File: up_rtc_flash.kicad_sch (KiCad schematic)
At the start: 0 parts

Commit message: add comments/todos for each schematics page
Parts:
- added Card?: PCIE-52P40H, PCIE-SMD_PCIE-52P40H, symbol eduboardv2:PCIE-52P40H
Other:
- note added: "UP-Connector, RTC and Flash - UP-Connector M.2: PCIE-52P40H - RTC: DS1307 (I2C) - CR2032 Battery: CR2032-BS-6-1 - Flash: W25Q128JVSIQ (Dual/Quad-SPI)"
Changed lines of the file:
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@@
     (company "Juventus Technikerschule")
   )
+  (text "UP-Connector, RTC and Flash\n- UP-Connector M.2: PCIE-52P40H\n- RTC: DS1307 (I2C)\n- CR2032 Battery: CR2032-BS-6-1\n- Flash: W25Q128JVSIQ (Dual/Quad-SPI)"
+    (at 13.97 24.13 0)
+    (effects (font (size 1.27 1.27)) (justify left bottom))
+  )
+  (symbol (lib_id "eduboardv2:PCIE-52P40H") (at 63.5 77.47 270) (unit 1)
+    (in_bom yes) (on_board yes) (fields_autoplaced)
+    (property "Reference" "Card?" (id 0) (at 66.2687 38.3372 90)
+      (effects (font (size 1.27 1.27)) (justify left))
+    )
+    (property "Value" "PCIE-52P40H" (id 1) (at 66.2687 40.8741 90)
+      (effects (font (size 1.27 1.27)) (justify left))
+    )
+    (property "Footprint" "PCIE-SMD_PCIE-52P40H" (id 2) (at 48.26 77.47 0)
+      (effects (font (size 1.27 1.27)) hide)
+    )
+    (property "Datasheet" "https://lcsc.com/product-detail/Connector-Card-Sockets_XUNPU-PCIE-52P40H_C266898.html" (id 3) (at 45.72 77.47 0)
+      (effects (font (size 1.27 1.27)) hide)
+    )
+    (property "Manufacturer" "XUNPU" (id 4) (at 43.18 77.47 0)
+      (effects (font (size 1.27 1.27)) hide)
+    )
+    (property "LCSC Part" "C266898" (id 5) (at 40.64 77.47 0)
+      (effects (font (size 1.27 1.27)) hide)
+    )
+    (property "JLC Part" "Extended Part" (id 6) (at 38.1 77.47 0)
+      (effects (font (size 1.27 1.27)) hide)
+    )
+    (pin "1")
+    (pin "10")
+    (pin "11")
+    (pin "12")
+    (pin "13")
+    (pin "14")
+    (pin "15")
+    (pin "16")
+    (pin "17")
+    (pin "18")
+    (pin "19")
+    (pin "2")
+    (pin "20")
+    (pin "21")
+    (pin "22")
+    (pin "23")
+    (pin "24")
+    (pin "25")
+    (pin "26")
+    (pin "27")
+    (pin "28")
+    (pin "29")
+    (pin "3")
+    (pin "30")
+    (pin "31")
+    (pin "32")
+    (pin "33")
+    (pin "34")
+    (pin "35")
+    (pin "36")
+    (pin "37")
+    (pin "38")
+    (pin "39")
+    (pin "4")
+    (pin "40")
+    (pin "41")
+    (pin "42")
+    (pin "43")
+    (pin "44")
+    (pin "45")
+    (pin "46")
+    (pin "47")
+    (pin "48")
+    (pin "49")
+    (pin "5")
+    (pin "50")
+    (pin "51")
+    (pin "52")
+    (pin "53")
+    (pin "54")
+    (pin "6")
+    (pin "7")
+    (pin "8")
+    (pin "9")
+  )
 )

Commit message: updated library, partly created power.kicad_sch
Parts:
- gave numbers to parts that had none: 1
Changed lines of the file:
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@@
   (symbol (lib_id "eduboardv2:PCIE-52P40H") (at 63.5 77.47 270) (unit 1)
     (in_bom yes) (on_board yes) (fields_autoplaced)
-    (property "Reference" "Card?" (id 0) (at 66.2687 38.3372 90)
+    (property "Reference" "X201" (id 0) (at 66.2687 36.83 90)
       (effects (font (size 1.27 1.27)) (justify left))
     )
-    (property "Value" "PCIE-52P40H" (id 1) (at 66.2687 40.8741 90)
+    (property "Value" "PCIE-52P40H" (id 1) (at 66.2687 39.37 90)
       (effects (font (size 1.27 1.27)) (justify left))
     )

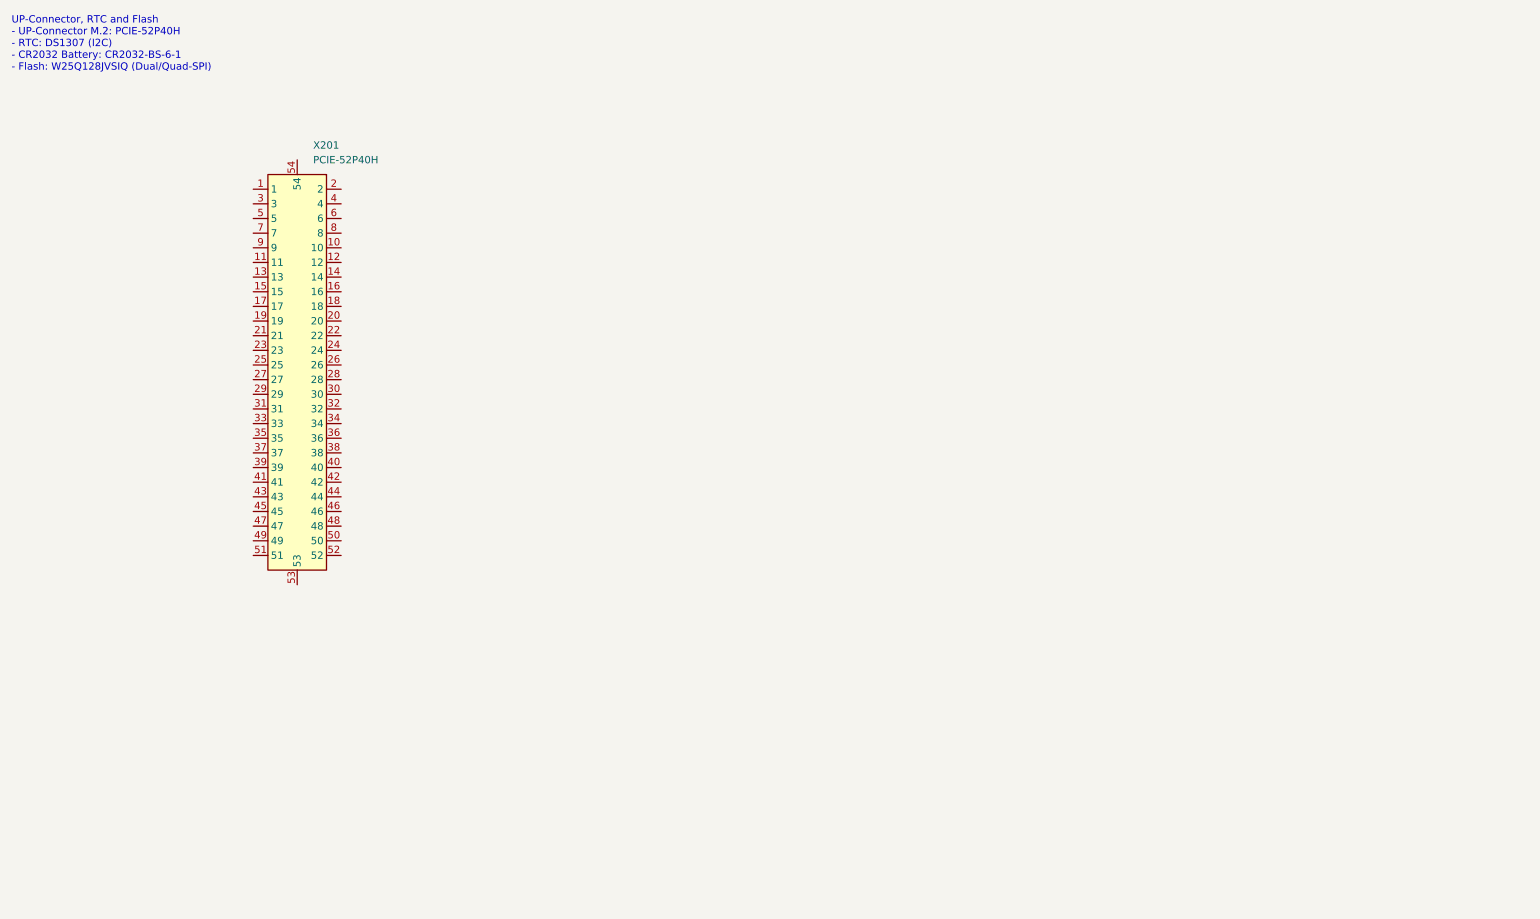
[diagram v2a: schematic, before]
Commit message: added up_rtc_flash.kicad_sch and finished others
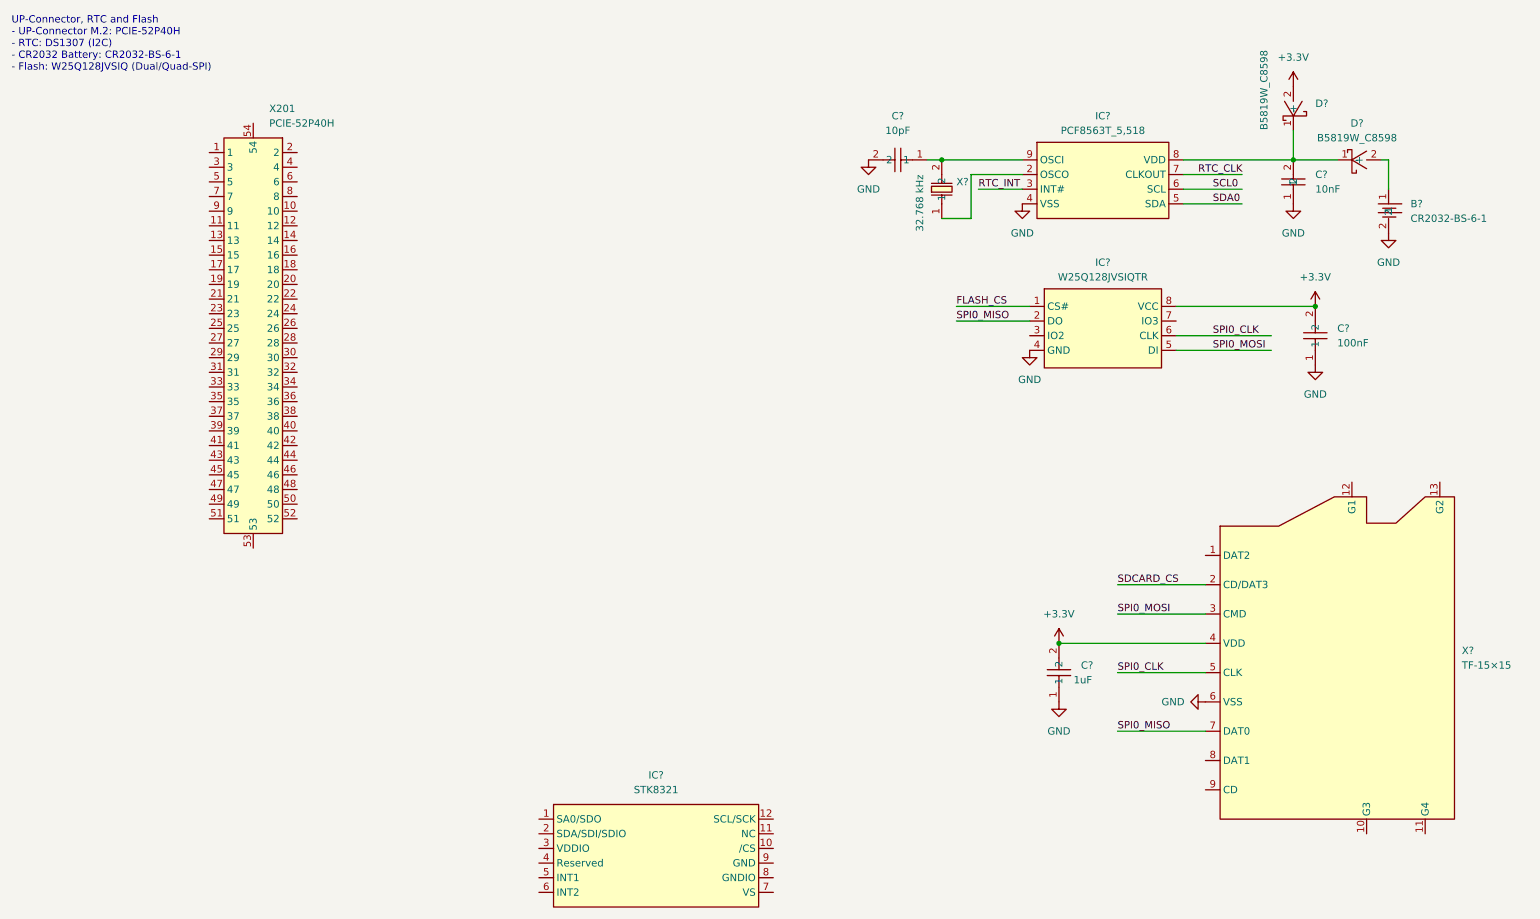
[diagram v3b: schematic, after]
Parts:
- added B?: CR2032-BS-6-1, BAT-TH_CR2032-BS-6-1, symbol eduboardv2:CR2032-BS-6-1
- added C?: 10pF, C0402, symbol eduboardv2:CL05C100JB5NNNC
- added C?: 10nF, C0402, symbol eduboardv2:CL05B103KB5NNNC
- added C?: 1uF, C0402, symbol eduboardv2:CL05A105KA5NQNC
- added C?: 100nF, C0402, symbol eduboardv2:CL05B104KB54PNC
- added D? (x2): B5819W_C8598, SOD-123_L2.7-W1.6-LS3.7-RD-1, symbol eduboardv2:B5819W_C8598
- added IC?: STK8321, LGA-12_L2.0-W2.0-P0.50-TR, symbol eduboardv2:STK8321
- added IC?: W25Q128JVSIQTR, SOIC-8_L5.3-W5.3-P1.27-LS8.0-BL, symbol eduboardv2:W25Q128JVSIQTR
- added IC?: PCF8563T_5,518, SOIC-8_L5.0-W4.0-P1.27-LS6.0-BL, symbol eduboardv2:PCF8563T_5,518
- added X?: TF-15×15, TF-SMD_TF-15-15, symbol eduboardv2:TF-15×15
- added X?: 32.768 kHz, FC-135R_L3.2-W1.5, symbol eduboardv2:Q13FC1350000400
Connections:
- new net: C?.2, D?.1 (-), D?.1 (-), IC?.8 (VDD)
- new net: B?.1, D?.2 (+)
- new net: C?.1, IC?.9 (OSCI), X?.2
- new net: IC?.2 (OSCO), X?.1
- new net +3.3V: C?.2, C?.2, D?.2 (+), IC?.8 (VCC), X?.4 (VDD)
- new net FLASH_CS: IC?.1 (CS#)
- new net GND: B?.2, C?.1, C?.1, C?.1, C?.2, IC?.4 (GND), IC?.4 (VSS), X?.6 (VSS)
- new net RTC_CLK: IC?.7 (CLKOUT)
- new net RTC_INT: IC?.3 (INT#)
- new net SCL0: IC?.6 (SCL)
- new net SDA0: IC?.5 (SDA)
- new net SDCARD_CS: X?.2 (CD/DAT3)
- new net SPI0_CLK: IC?.6 (CLK), X?.5 (CLK)
- new net SPI0_MISO: IC?.2 (DO), X?.7 (DAT0)
- new net SPI0_MOSI: IC?.5 (DI), X?.3 (CMD)
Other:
- moved on the sheet: X201

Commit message: added more components
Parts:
- gave numbers to parts that had none: 12
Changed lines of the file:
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@@
   (symbol (lib_id "eduboardv2:STK8321") (at 125.73 160.02 0) (unit 1)
     (in_bom yes) (on_board yes) (fields_autoplaced)
-    (property "Reference" "IC?" (id 0) (at 125.73 146.05 0))
+    (property "Reference" "IC201" (id 0) (at 125.73 146.05 0))
     (property "Value" "STK8321" (id 1) (at 125.73 148.59 0))
     (property "Footprint" "LGA-12_L2.0-W2.0-P0.50-TR" (id 2) (at 125.73 173.99 0)
@@
   (symbol (lib_id "eduboardv2:B5819W_C8598") (at 247.65 39.37 0) (unit 1)
     (in_bom yes) (on_board yes) (fields_autoplaced)
-    (property "Reference" "D?" (id 0) (at 247.269 33.02 0))
+    (property "Reference" "D202" (id 0) (at 247.269 33.02 0))
     (property "Value" "B5819W_C8598" (id 1) (at 247.269 35.56 0))
     (property "Footprint" "SOD-123_L2.7-W1.6-LS3.7-RD-1" (id 2) (at 247.65 46.99 0)
@@
   (symbol (lib_id "power:GND") (at 220.98 133.35 270) (unit 1)
     (in_bom yes) (on_board yes)
-    (property "Reference" "#PWR?" (id 0) (at 214.63 133.35 0)
+    (property "Reference" "#PWR0206" (id 0) (at 214.63 133.35 0)
       (effects (font (size 1.27 1.27)) hide)
     )
@@
   (symbol (lib_id "eduboardv2:W25Q128JVSIQTR") (at 203.2 68.58 0) (unit 1)
     (in_bom yes) (on_board yes) (fields_autoplaced)
-    (property "Reference" "IC?" (id 0) (at 203.2 57.15 0))
+    (property "Reference" "IC203" (id 0) (at 203.2 57.15 0))
     (property "Value" "W25Q128JVSIQTR" (id 1) (at 203.2 59.69 0))
     (property "Footprint" "SOIC-8_L5.3-W5.3-P1.27-LS8.0-BL" (id 2) (at 203.2 80.01 0)
@@
   (symbol (lib_id "power:GND") (at 190.5 72.39 0) (unit 1)
     (in_bom yes) (on_board yes) (fields_autoplaced)
-    (property "Reference" "#PWR?" (id 0) (at 190.5 78.74 0)
+    (property "Reference" "#PWR0203" (id 0) (at 190.5 78.74 0)
       (effects (font (size 1.27 1.27)) hide)
     )
@@
   (symbol (lib_id "eduboardv2:CL05C100JB5NNNC") (at 167.64 39.37 180) (unit 1)
     (in_bom yes) (on_board yes) (fields_autoplaced)
-    (property "Reference" "C?" (id 0) (at 167.64 31.75 0))
+    (property "Reference" "C201" (id 0) (at 167.64 31.75 0))
     (property "Value" "10pF" (id 1) (at 167.64 34.29 0))
     (property "Footprint" "C0402" (id 2) (at 167.64 31.75 0)
@@
   (symbol (lib_id "eduboardv2:CR2032-BS-6-1") (at 252.73 48.26 270) (unit 1)
     (in_bom yes) (on_board yes) (fields_autoplaced)
-    (property "Reference" "B?" (id 0) (at 256.54 46.9899 90)
+    (property "Reference" "B201" (id 0) (at 256.54 46.9899 90)
       (effects (font (size 1.27 1.27)) (justify left))
     )
@@
   (symbol (lib_id "eduboardv2:CL05B103KB5NNNC") (at 236.22 43.18 90) (unit 1)
     (in_bom yes) (on_board yes) (fields_autoplaced)
-    (property "Reference" "C?" (id 0) (at 240.03 41.9099 90)
+    (property "Reference" "C203" (id 0) (at 240.03 41.9099 90)
       (effects (font (size 1.27 1.27)) (justify right))
     )
@@
   (symbol (lib_id "power:GND") (at 189.23 46.99 0) (unit 1)
     (in_bom yes) (on_board yes) (fields_autoplaced)
-    (property "Reference" "#PWR?" (id 0) (at 189.23 53.34 0)
+    (property "Reference" "#PWR0202" (id 0) (at 189.23 53.34 0)
       (effects (font (size 1.27 1.27)) hide)
     )
@@
   (symbol (lib_id "eduboardv2:CL05A105KA5NQNC") (at 195.58 128.27 90) (unit 1)
     (in_bom yes) (on_board yes)
-    (property "Reference" "C?" (id 0) (at 199.39 126.9999 90)
+    (property "Reference" "C202" (id 0) (at 199.39 126.9999 90)
       (effects (font (size 1.27 1.27)) (justify right))
     )
@@
   (symbol (lib_id "eduboardv2:B5819W_C8598") (at 236.22 30.48 90) (unit 1)
     (in_bom yes) (on_board yes)
-    (property "Reference" "D?" (id 0) (at 240.03 29.5909 90)
+    (property "Reference" "D201" (id 0) (at 240.03 29.5909 90)
       (effects (font (size 1.27 1.27)) (justify right))
     )
@@
   (symbol (lib_id "power:+3.3V") (at 240.03 64.77 0) (unit 1)
     (in_bom yes) (on_board yes) (fields_autoplaced)
-    (property "Reference" "#PWR?" (id 0) (at 240.03 68.58 0)
+    (property "Reference" "#PWR0209" (id 0) (at 240.03 68.58 0)
       (effects (font (size 1.27 1.27)) hide)
     )
@@
   (symbol (lib_id "power:+3.3V") (at 195.58 123.19 0) (unit 1)
     (in_bom yes) (on_board yes) (fields_autoplaced)
-    (property "Reference" "#PWR?" (id 0) (at 195.58 127 0)
+    (property "Reference" "#PWR0204" (id 0) (at 195.58 127 0)
       (effects (font (size 1.27 1.27)) hide)
     )
@@
   (symbol (lib_id "power:GND") (at 162.56 39.37 0) (unit 1)
     (in_bom yes) (on_board yes) (fields_autoplaced)
-    (property "Reference" "#PWR?" (id 0) (at 162.56 45.72 0)
+    (property "Reference" "#PWR0201" (id 0) (at 162.56 45.72 0)
       (effects (font (size 1.27 1.27)) hide)
     )
@@
   (symbol (lib_id "eduboardv2:TF-15×15") (at 240.03 125.73 0) (unit 1)
     (in_bom yes) (on_board yes) (fields_autoplaced)
-    (property "Reference" "X?" (id 0) (at 265.43 124.4599 0)
+    (property "Reference" "X203" (id 0) (at 265.43 124.4599 0)
       (effects (font (size 1.27 1.27)) (justify left))
     )
@@
   (symbol (lib_id "power:+3.3V") (at 236.22 26.67 0) (unit 1)
     (in_bom yes) (on_board yes) (fields_autoplaced)
-    (property "Reference" "#PWR?" (id 0) (at 236.22 30.48 0)
+    (property "Reference" "#PWR0207" (id 0) (at 236.22 30.48 0)
       (effects (font (size 1.27 1.27)) hide)
     )
@@
   (symbol (lib_id "power:GND") (at 240.03 74.93 0) (unit 1)
     (in_bom yes) (on_board yes) (fields_autoplaced)
-    (property "Reference" "#PWR?" (id 0) (at 240.03 81.28 0)
+    (property "Reference" "#PWR0210" (id 0) (at 240.03 81.28 0)
       (effects (font (size 1.27 1.27)) hide)
     )
@@
   (symbol (lib_id "eduboardv2:Q13FC1350000400") (at 175.26 44.45 90) (unit 1)
     (in_bom yes) (on_board yes)
-    (property "Reference" "X?" (id 0) (at 177.8 43.1799 90)
+    (property "Reference" "X202" (id 0) (at 177.8 43.1799 90)
       (effects (font (size 1.27 1.27)) (justify right))
     )
@@
   (symbol (lib_id "eduboardv2:CL05B104KB54PNC") (at 240.03 69.85 90) (unit 1)
     (in_bom yes) (on_board yes) (fields_autoplaced)
-    (property "Reference" "C?" (id 0) (at 243.84 68.5799 90)
+    (property "Reference" "C204" (id 0) (at 243.84 68.5799 90)
       (effects (font (size 1.27 1.27)) (justify right))
     )
@@
   (symbol (lib_id "power:GND") (at 252.73 52.07 0) (unit 1)
     (in_bom yes) (on_board yes) (fields_autoplaced)
-    (property "Reference" "#PWR?" (id 0) (at 252.73 58.42 0)
+    (property "Reference" "#PWR0211" (id 0) (at 252.73 58.42 0)
       (effects (font (size 1.27 1.27)) hide)
     )
@@
   (symbol (lib_id "eduboardv2:PCF8563T_5,518") (at 203.2 43.18 0) (unit 1)
     (in_bom yes) (on_board yes) (fields_autoplaced)
-    (property "Reference" "IC?" (id 0) (at 203.2 31.75 0))
+    (property "Reference" "IC202" (id 0) (at 203.2 31.75 0))
     (property "Value" "PCF8563T_5,518" (id 1) (at 203.2 34.29 0))
     (property "Footprint" "SOIC-8_L5.0-W4.0-P1.27-LS6.0-BL" (id 2) (at 203.2 54.61 0)
@@
   (symbol (lib_id "power:GND") (at 195.58 133.35 0) (unit 1)
     (in_bom yes) (on_board yes) (fields_autoplaced)
-    (property "Reference" "#PWR?" (id 0) (at 195.58 139.7 0)
+    (property "Reference" "#PWR0205" (id 0) (at 195.58 139.7 0)
       (effects (font (size 1.27 1.27)) hide)
     )
@@
   (symbol (lib_id "power:GND") (at 236.22 46.99 0) (unit 1)
     (in_bom yes) (on_board yes) (fields_autoplaced)
-    (property "Reference" "#PWR?" (id 0) (at 236.22 53.34 0)
-      (effects (font (size 1.27 1.27)) hide)
-    )
+    (property "Reference" "#PWR0208" (id 0) (at 236.22 53.34 0)
+      (effects (font (size 1.27 1.27)) hide)
+    )

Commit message: beautified the library
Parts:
- X201: MPN (none) -> PCIE-52P40H
